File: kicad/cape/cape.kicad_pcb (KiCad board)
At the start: 2 copper layers, 86.4 x 54.6 mm, 18 parts, among them M1 HSR-2648CR, P1 BeagleBone_Black_Header, P2 BeagleBone_Black_Header, U1 BNO055, U2 S13V10F5, U3 stepper_breakout, U4 A4988

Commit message: Working on post-build payload changes
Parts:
- removed U3: stepper_breakout, Connector_PinSocket_2.54mm:PinSocket_1x04_P2.54mm_Vertical
- removed U4: A4988, payload_footprint_library:Pololu_Breakout-16_15.2x20.3mm
- added C4: 220 uF, Capacitor_THT:C_Radial_D8.0mm_H7.0mm_P3.50mm, F.Cu at (111.0, 73.1)
- C1: value 100 uF -> 220 uF; footprint Capacitor_THT:C_Radial_D10.0mm_H16.0mm_P5.00mm -> Capacitor_THT:C_Radial_D8.0mm_H11.5mm_P3.50mm
- C3: value 100 uF -> 220 uF; footprint Capacitor_THT:C_Radial_D10.0mm_H16.0mm_P5.00mm -> Capacitor_THT:C_Radial_D8.0mm_H7.0mm_P3.50mm
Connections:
- net /GPIO[22] renamed /PWM2A
- net /GPIO[40] renamed /PWM1A
- net /GPIO[51] renamed /PWM1B
- net /LCD.DATA[0] renamed /LCD_DATA2
- net /LCD.DATA[2] renamed /LCD_DATA4
- net /LCD.DATA[4] renamed /LCD_DATA6
- net /LCD.DATA[6] renamed /LCD_DATA8
- net /LCD.DATA[8] renamed /LCD_DATA12
- P2 pad 13: /GPIO[23] -> /PWM2B
- P2 pad 45: GNDD -> /LCD_DATA0
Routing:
- net +3.3V: track 88.0 -> 63.4 mm
- net /GPIO[47]: track 23.7 -> 0.00 mm
- net /GPIO[65]: track 21.1 -> 0.00 mm
- net /GPIO[27]: track 20.1 -> 0.00 mm
- net /+7.4V: track 56.5 -> 37.7 mm
- net /GPIO[61]: track 13.4 -> 0.00 mm
- net Net-(U3-Pad4): track 5.51 -> 0.00 mm
- net Net-(U3-Pad3): track 5.51 -> 0.00 mm
- net Net-(U3-Pad2): track 5.51 -> 0.00 mm
- net Net-(U3-Pad1): track 5.51 -> 0.00 mm
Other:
- board text removed: "1A"
- board text removed: "1B"
- board text removed: "2A"
- board text removed: "2B"

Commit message: Cape v1-5
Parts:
- added G***: LOGO, payload_footprint_library:logo, F.Cu at (105.7, 57.0)
- added M2: Motor_Servo_Feedback, Connector_PinHeader_2.54mm:PinHeader_1x04_P2.54mm_Vertical, F.Cu at (87.3, 41.6)
- M1: value HSR-2648CR -> Motor_Servo_Feedback; footprint Connector_PinSocket_2.54mm:PinSocket_1x03_P2.54mm_Vertical -> Connector_PinHeader_2.54mm:PinHeader_1x04_P2.54mm_Vertical
- R1, R2: footprint Resistor_THT:R_Axial_DIN0207_L6.3mm_D2.5mm_P10.16mm_Horizontal -> Resistor_THT:R_Axial_DIN0207_L6.3mm_D2.5mm_P15.24mm_Horizontal
- moved M1 17.5 mm to (105.1, 41.6)
- moved C3 11.4 mm to (93.7, 65.7)
- moved C4 11.1 mm to (100.0, 74.6)
- moved R2 10.5 mm to (111.4, 74.6)
- moved R1 10.5 mm to (111.4, 69.5)
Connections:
- M1 pad 1: /GPIO[23] -> /PWM2A
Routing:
- net /+7.4V: track 37.7 -> 63.5 mm
- net /GPIO[45]: track 0.00 -> 11.5 mm
- net +5V: track 30.8 -> 38.4 mm
- net /I2C2.SDA: track 46.5 -> 38.8 mm
- net /PWM2A: track 0.00 -> 7.11 mm
- net /PWM2B: track 0.00 -> 6.47 mm
- net /GPIO[23]: track 6.32 -> 0.00 mm
- net /I2C2.SCL: track 50.8 -> 44.6 mm
- net +3.3V: track 63.4 -> 59.0 mm
- net /GPIO[27]: track 0.00 -> 4.26 mm
- net /GPIO[117]: track 45.7 -> 42.0 mm
- net /GPIO_112: track 62.1 -> 62.9 mm
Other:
- board text added: "FDBK"

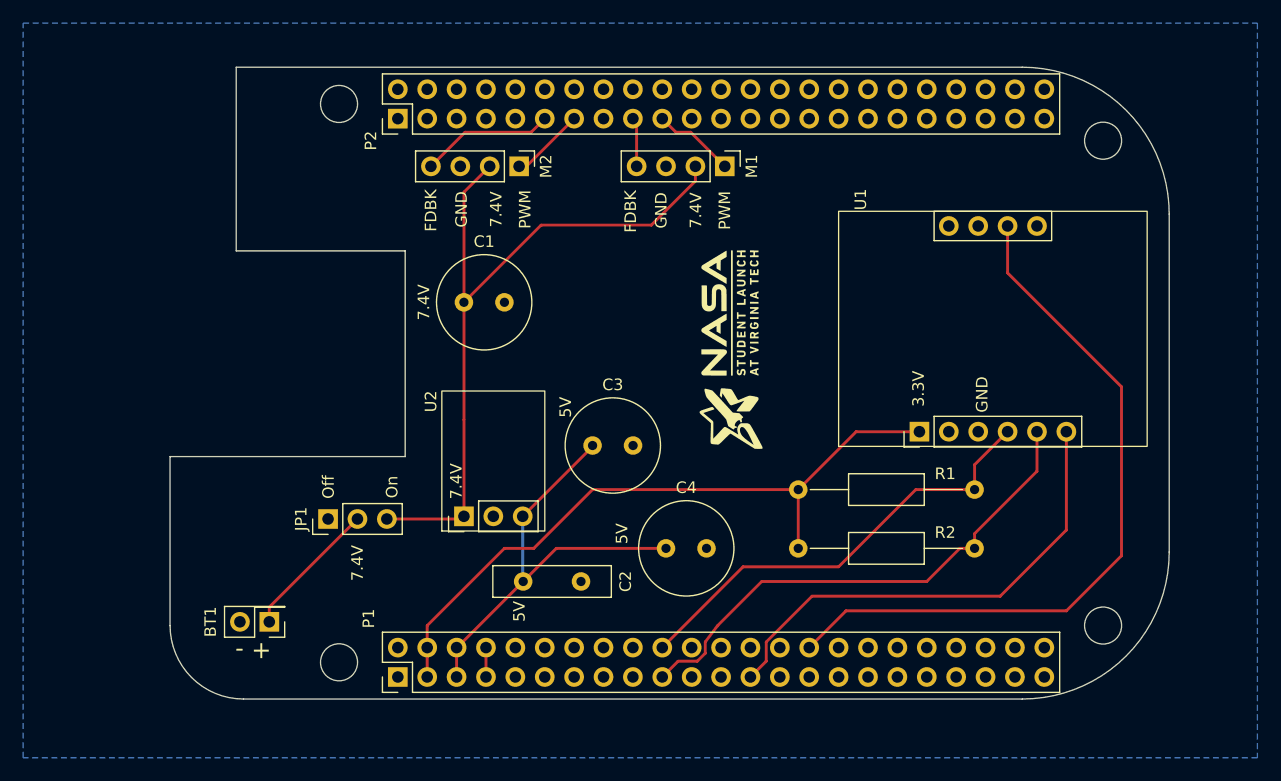
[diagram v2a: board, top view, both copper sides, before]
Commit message: Finished cape v1-5
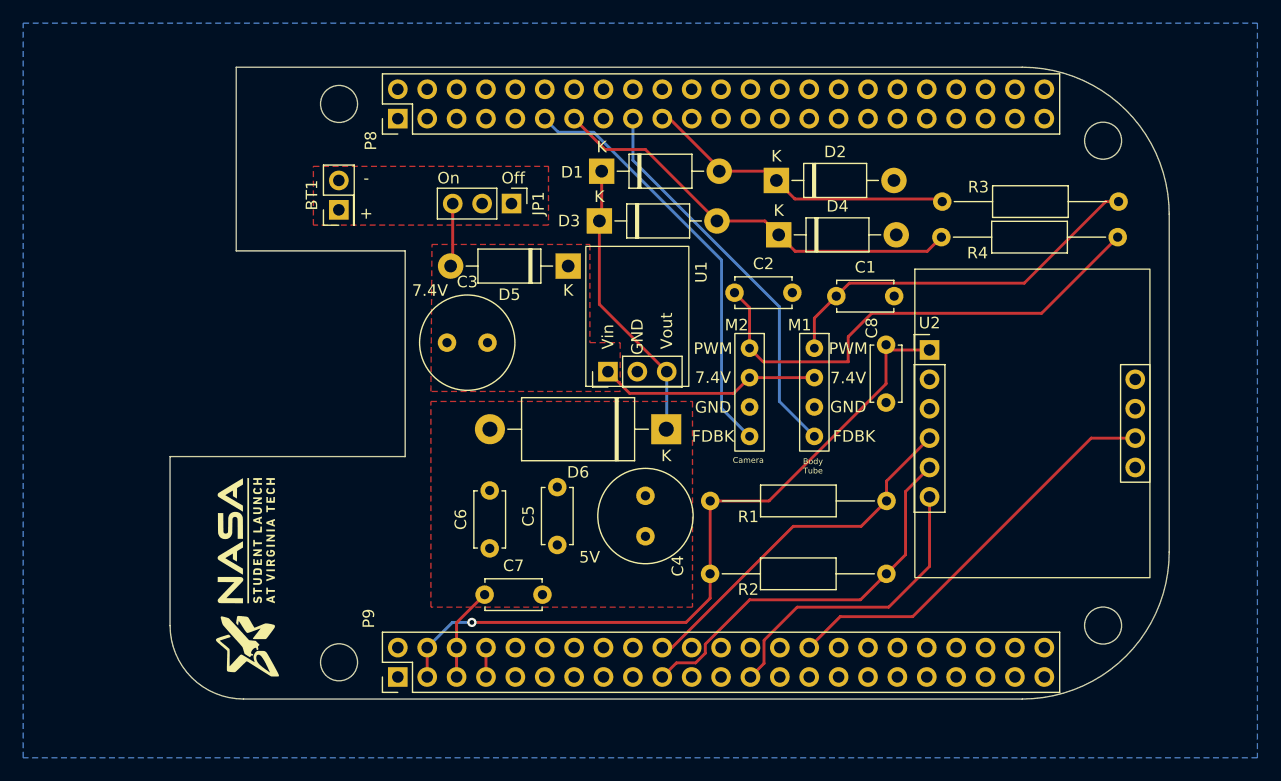
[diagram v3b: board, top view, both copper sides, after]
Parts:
- removed G***: LOGO, payload_footprint_library:logo
- added C5: 100 nF, Capacitor_THT:C_Disc_D4.7mm_W2.5mm_P5.00mm, F.Cu at (90.6, 74.3)
- added C6: 10 nF, Capacitor_THT:C_Disc_D4.7mm_W2.5mm_P5.00mm, F.Cu at (84.8, 74.6)
- added C7: 1 nF, Capacitor_THT:C_Disc_D4.7mm_W2.5mm_P5.00mm, F.Cu at (84.3, 78.6)
- added C8: 100 nF, Capacitor_THT:C_Disc_D4.7mm_W2.5mm_P5.00mm, F.Cu at (119.0, 57.0)
- added D1: 1N5817, Diode_THT:D_DO-41_SOD81_P10.16mm_Horizontal, F.Cu at (94.4, 42.0)
- added D2: 1N5817, Diode_THT:D_DO-41_SOD81_P10.16mm_Horizontal, F.Cu at (109.5, 42.8)
- added D3: 1N5817, Diode_THT:D_DO-41_SOD81_P10.16mm_Horizontal, F.Cu at (94.2, 46.3)
- added D4: 1N5817, Diode_THT:D_DO-41_SOD81_P10.16mm_Horizontal, F.Cu at (109.7, 47.5)
- added D5: 1N5817, Diode_THT:D_DO-41_SOD81_P10.16mm_Horizontal, F.Cu at (91.5, 50.2)
- added D6: 1N5339B, Diode_THT:D_DO-201_P15.24mm_Horizontal, F.Cu at (100.0, 64.3)
- added R3: 1K, Resistor_THT:R_Axial_DIN0207_L6.3mm_D2.5mm_P15.24mm_Horizontal, F.Cu at (123.9, 44.6)
- added R4: 1K, Resistor_THT:R_Axial_DIN0207_L6.3mm_D2.5mm_P15.24mm_Horizontal, F.Cu at (123.8, 47.7)
- added U3: LOGO_SMALL, payload_footprint_library:logo, F.Cu at (63.9, 76.7)
- C1: value 220 uF -> 100 nF; footprint Capacitor_THT:C_Radial_D8.0mm_H11.5mm_P3.50mm -> Capacitor_THT:C_Disc_D4.7mm_W2.5mm_P5.00mm
- C2: value 10 nF -> 100 nF; footprint Capacitor_THT:C_Disc_D10.0mm_W2.5mm_P5.00mm -> Capacitor_THT:C_Disc_D4.7mm_W2.5mm_P5.00mm
- C3: value 220 uF -> 100 uF; footprint Capacitor_THT:C_Radial_D8.0mm_H7.0mm_P3.50mm -> Capacitor_THT:C_Radial_D8.0mm_H11.5mm_P3.50mm
- C4: value 220 uF -> 100 uF
- M1, M2: footprint Connector_PinHeader_2.54mm:PinHeader_1x04_P2.54mm_Vertical -> payload_footprint_library:FeedbackServo
- U1: value BNO055 -> S13V20F5; footprint payload_footprint_library:BNO055 -> payload_footprint_library:S13V10F5
- U2: value S13V10F5 -> BNO055; footprint payload_footprint_library:S13V10F5 -> payload_footprint_library:BNO055
- moved U2 42.7 mm to (122.8, 57.5), turned to 0 degrees
- moved BT1 36.1 mm to (71.7, 45.3), turned to 90 degrees
- moved C1 32.2 mm to (114.7, 52.8)
- moved JP1 31.5 mm to (86.6, 44.8), turned to -90 degrees
- moved C2 30.9 mm to (105.9, 52.5)
- moved U1 27.4 mm to (95.0, 59.3)
- moved M2 25.4 mm to (107.2, 57.3)
- moved M1 17.5 mm to (112.8, 57.3)
- moved C3 15.4 mm to (81.1, 56.8)
- moved R2 7.93 mm to (103.8, 76.8)
- moved R1 7.67 mm to (103.8, 70.5)
- moved C4 2.06 mm to (98.2, 73.6), turned to 90 degrees
- renumbered P2 to P8, P1 to P9
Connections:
- net Net-(BT1-Pad1) renamed /batt
- C1 pad 1: /+7.4V -> Net-(C1-Pad1)
- C2 pad 1: +5V -> Net-(C2-Pad1)
- C3 pad 1: +5V -> /+7.4V
- JP1 pad 3: /+7.4V -> Net-(D5-Pad2)
- M1 pad 1: /PWM2A -> Net-(C1-Pad1)
- M2 pad 1: /PWM2B -> Net-(C2-Pad1)
- U1 pad 1: +3.3V -> /+7.4V
- U1 pad 2: unconnected-(U1-Pad2) -> GNDD
- U1 pad 3: GNDD -> +5V
- U2 pad 1: /+7.4V -> +3.3V
- U2 pad 2: GNDD -> unconnected-(U2-Pad2)
- U2 pad 3: +5V -> GNDD
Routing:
- net /+7.4V: track 63.5 -> 19.2 mm
- net Net-(C2-Pad1): track 0.00 -> 43.4 mm
- net Net-(C1-Pad1): track 0.00 -> 33.1 mm
- net /PWM2B: track 6.47 -> 37.0 mm
- net /GPIO[27]: track 4.26 -> 34.0 mm
- net /GPIO_112: track 62.9 -> 35.7 mm
- net /GPIO[45]: track 11.5 -> 36.6 mm
- net /PWM2A: track 7.11 -> 27.1 mm
- net /GPIO[117]: track 42.0 -> 26.6 mm
- net /batt: track 12.0 -> 0.00 mm
- net /I2C2.SCL: track 44.6 -> 34.3 mm
- net /I2C2.SDA: track 38.8 -> 31.6 mm
- net +5V: track 38.4 -> 32.9 mm
- net Net-(D5-Pad2): track 0.00 -> 5.48 mm
- net +3.3V: track 59.0 -> 63.9 mm, vias 0 -> 1
- added copper zone on F.Cu, net +5V
- added copper zone on F.Cu, net /+7.4V
- added copper zone on F.Cu, net /batt
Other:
- board text added: "+"
- board text added: "-"
- board text added: "Body Tube"
- board text added: "Camera"
- board text removed: "+ -"
- board text removed: "3.3V"
- board text removed: "FDBK"
- board text removed: "GND"
- board text removed: "PWM"
